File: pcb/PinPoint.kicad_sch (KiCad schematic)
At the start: 2 parts, among them U1 E73-2G4M08S-52833

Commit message: Create board outline, change battery holder
Signed-off-by: Devnol <pgkoutsoumanis@gmail.com>
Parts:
- BT1: footprint Battery:BatteryHolder_Multicomp_BC-2001_1x2032 -> Battery:BatteryHolder_Keystone_3034_1x20mm
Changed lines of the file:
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@@
 			)
 		)
-		(property "Footprint" "Battery:BatteryHolder_Multicomp_BC-2001_1x2032"
+		(property "Footprint" "Battery:BatteryHolder_Keystone_3034_1x20mm"
 			(at 59.69 84.836 90)
 			(effects

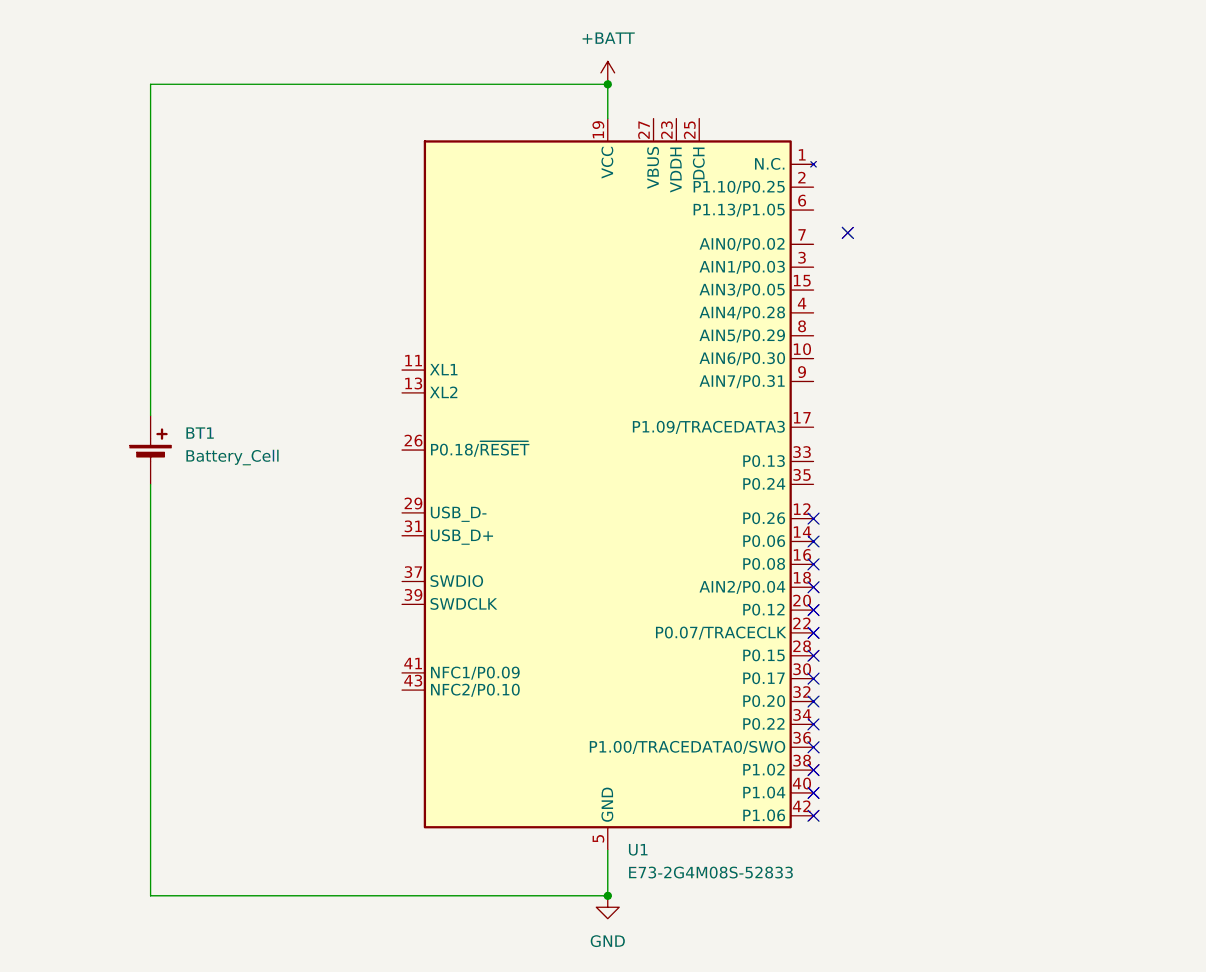
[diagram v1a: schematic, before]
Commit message: Add screw holes, debug port
Signed-off-by: Devnol <pgkoutsoumanis@gmail.com>
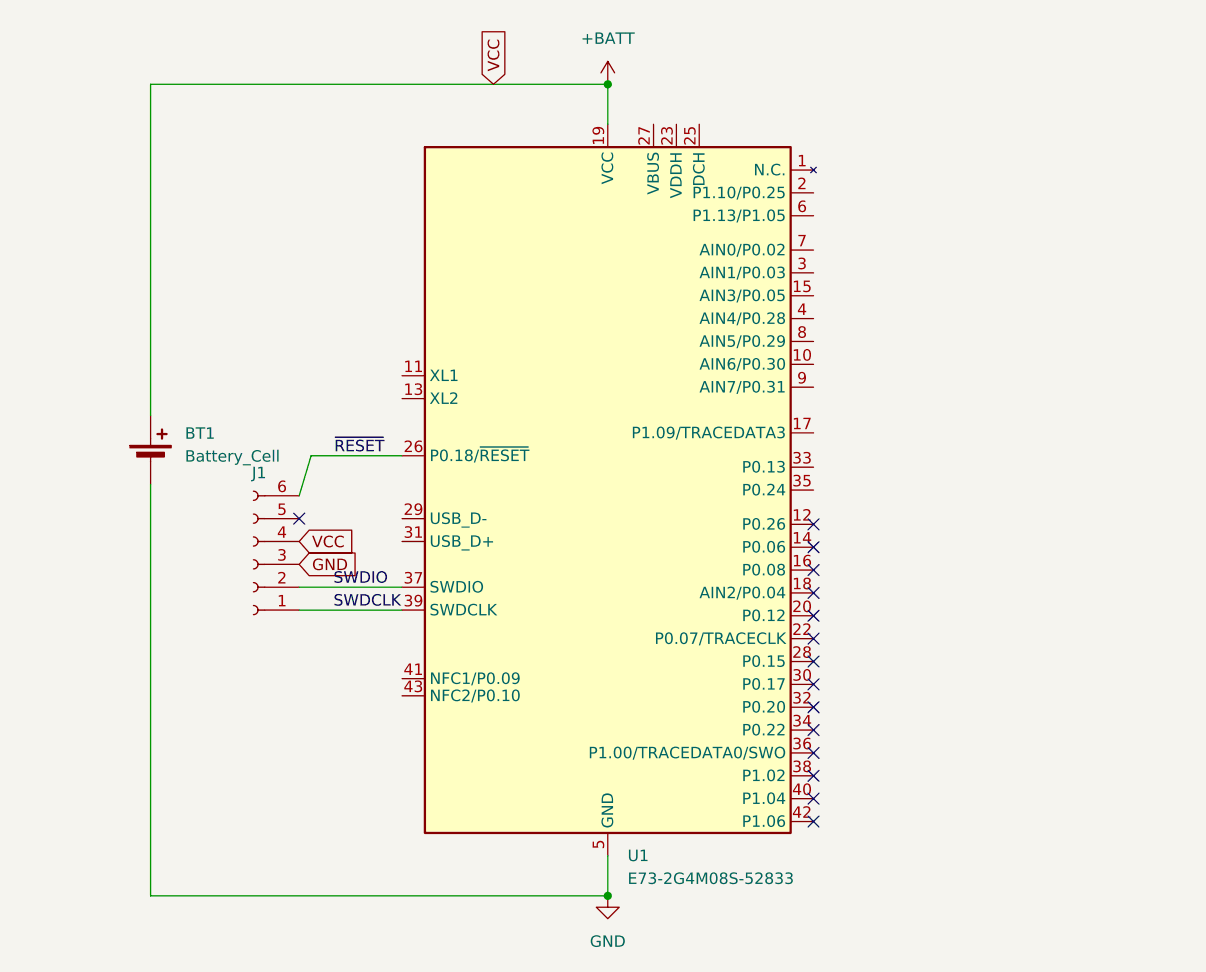
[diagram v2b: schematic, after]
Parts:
- added J1: ~, Connector_PinHeader_2.54mm:PinHeader_2x03_P2.54mm_Horizontal, symbol Connector:Conn_01x06_Socket
- U1: IC Datasheet (none) -> ${KIPRJMOD}/../docs/nRF52833_PS_v1.7.pdf
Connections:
- net +BATT: now also J1.4 (Pin_4)
- net GND: now also J1.3 (Pin_3)
- net ~{RESET}: now reaches U1.26 (P0.18/~{RESET})
- net ~{RESET}: now also J1.6 (Pin_6)
- net SWDIO: now reaches U1.37 (SWDIO)
- net SWDIO: now also J1.2 (Pin_2)
- net SWDCLK: now reaches U1.39 (SWDCLK)
- net SWDCLK: now also J1.1 (Pin_1)
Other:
- moved on the sheet: U1

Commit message: Add buzzer, include todo list for board features
Signed-off-by: Devnol <pgkoutsoumanis@gmail.com>
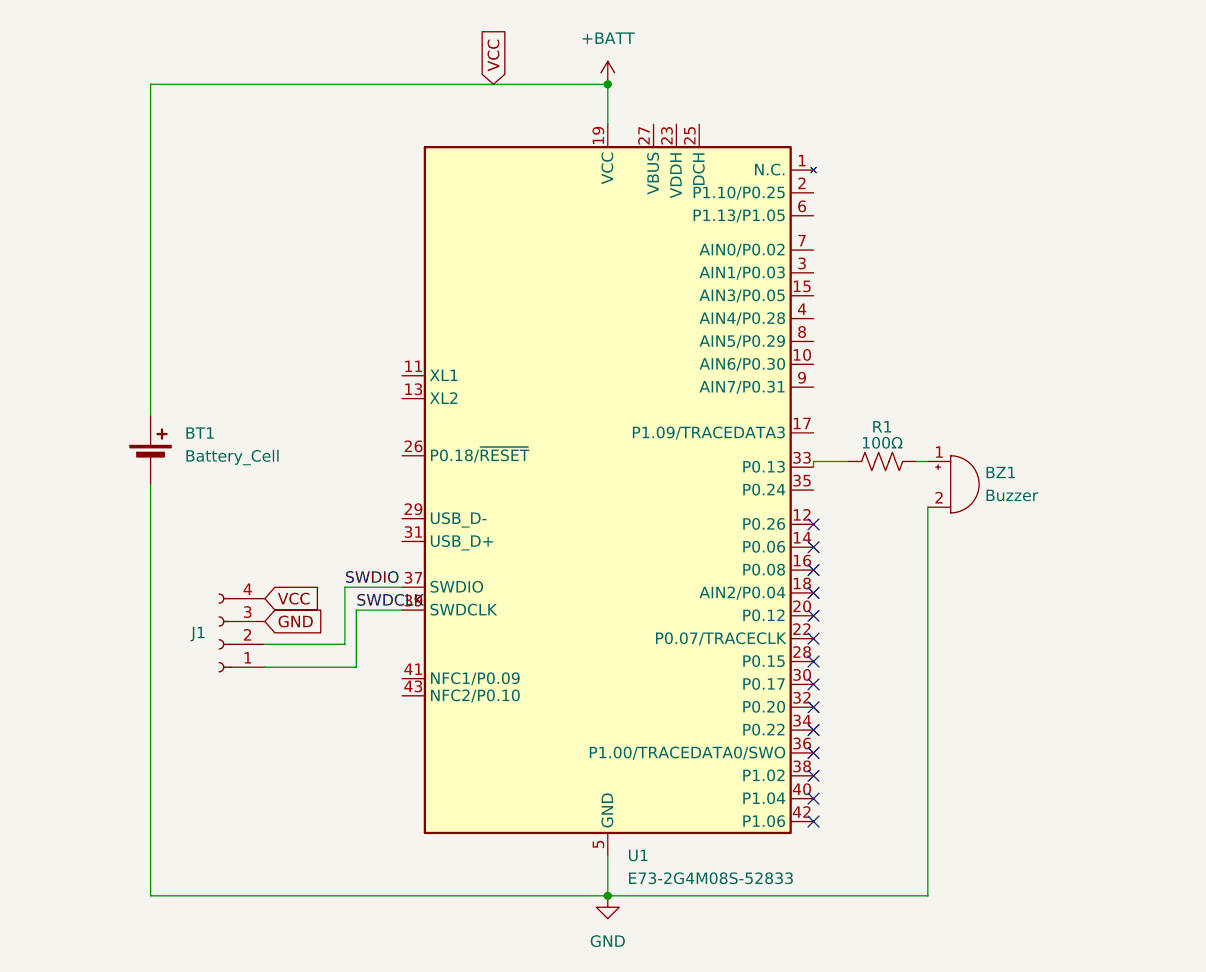
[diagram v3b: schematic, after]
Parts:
- added BZ1: Buzzer, Buzzer_Beeper:Buzzer_Murata_PKMCS0909E, symbol Device:Buzzer
- added R1: 100Ω, Resistor_SMD:R_0603_1608Metric, symbol Device:R_US
- J1: footprint Connector_PinHeader_2.54mm:PinHeader_2x03_P2.54mm_Horizontal -> Connector_PinHeader_2.54mm:PinHeader_1x04_P2.54mm_Vertical; symbol Connector:Conn_01x06_Socket -> Connector:Conn_01x04_Socket
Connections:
- net GND: now also BZ1.2 (-)
- net at U1.33 (P0.13): now also R1.1
- net ~{RESET}: no longer names the net of U1.26 (P0.18/~{RESET})
- net ~{RESET}: no longer J1.6 (Pin_6)
- new net: BZ1.1 (+), R1.2
- no-connect marks 15 -> 14
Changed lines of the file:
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@@
-	)
-	(no_connect
-		(at 76.2 92.71)
 	)
 	(no_connect
@@
 	(wire
 		(pts
-			(xy 77.5257 85.725) (xy 87.63 85.725)
+			(xy 82.55 109.22) (xy 82.55 102.87)
+		)
+		(stroke
+			(width 0)
+			(type default)
+		)
+	)
+	(wire
+		(pts
+			(xy 82.55 102.87) (xy 87.63 102.87)
 		)
 		(stroke
@@
 	(wire
 		(pts
-			(xy 77.5257 85.725) (xy 76.2 90.17)
-		)
-		(stroke
-			(width 0)
-			(type default)
-		)
-	)
-	(wire
-		(pts
 			(xy 59.69 81.28) (xy 59.69 44.45)
 		)
@@
 	(wire
 		(pts
+			(xy 81.28 106.68) (xy 81.28 100.33)
+		)
+		(stroke
+			(width 0)
+			(type default)
+		)
+	)
+	(wire
+		(pts
+			(xy 133.35 86.36) (xy 133.35 86.995)
+		)
+		(stroke
+			(width 0)
+			(type default)
+		)
+	)
+	(wire
+		(pts
+			(xy 144.78 86.36) (xy 146.05 86.36)
+		)
+		(stroke
+			(width 0)
+			(type default)
+		)
+	)
+	(wire
+		(pts
 			(xy 59.69 134.62) (xy 110.49 134.62)
 		)
@@
 	(wire
 		(pts
+			(xy 146.05 134.62) (xy 110.49 134.62)
+		)
+		(stroke
+			(width 0)
+			(type default)
+		)
+	)
+	(wire
+		(pts
 			(xy 110.49 134.62) (xy 110.49 130.175)
 		)
@@
 	(wire
 		(pts
-			(xy 76.2 102.87) (xy 87.63 102.87)
+			(xy 72.39 109.22) (xy 82.55 109.22)
 		)
 		(stroke
@@
 	(wire
 		(pts
-			(xy 76.2 100.33) (xy 87.63 100.33)
+			(xy 81.28 100.33) (xy 87.63 100.33)
+		)
+		(stroke
+			(width 0)
+			(type default)
+		)
+	)
+	(wire
+		(pts
+			(xy 72.39 106.68) (xy 81.28 106.68)
+		)
+		(stroke
+			(width 0)
+			(type default)
+		)
+	)
+	(wire
+		(pts
+			(xy 146.05 91.44) (xy 146.05 134.62)
+		)
+		(stroke
+			(width 0)
+			(type default)
+		)
+	)
+	(wire
+		(pts
+			(xy 133.35 86.36) (xy 137.16 86.36)
 		)
 		(stroke
@@
 	)
 	(label "SWDCLK"
-		(at 80.01 102.87 0)
+		(at 82.55 102.87 0)
 		(fields_autoplaced yes)
 		(effects
@@
 	)
 	(label "SWDIO"
-		(at 80.01 100.33 0)
+		(at 81.28 100.33 0)
 		(fields_autoplaced yes)
 		(effects
@@
 		)
 	)
-	(label "~{RESET}"
-		(at 80.0916 85.725 0)
+	(global_label "GND"
+		(shape input)
+		(at 72.39 104.14 0)
 		(fields_autoplaced yes)
 		(effects
@@
 				(size 1.27 1.27)
 			)
-			(justify left bottom)
-		)
-	)
-	(global_label "GND"
+			(justify left)
+		)
+		(property "Intersheetrefs" "${INTERSHEET_REFS}"
+			(at 79.2457 104.14 0)
+			(effects
+				(font
+					(size 1.27 1.27)
+				)
+				(justify left)
+				(hide yes)
+			)
+		)
+	)
+	(global_label "VCC"
 		(shape input)
-		(at 76.2 97.79 0)
+		(at 97.79 44.45 90)
 		(fields_autoplaced yes)
 		(effects
@@
 		)
 		(property "Intersheetrefs" "${INTERSHEET_REFS}"
-			(at 83.0557 97.79 0)
+			(at 97.79 37.8362 90)
 			(effects
 				(font
@@
 	(global_label "VCC"
 		(shape input)
-		(at 97.79 44.45 90)
+		(at 72.39 101.6 0)
 		(fields_autoplaced yes)
 		(effects
@@
 		)
 		(property "Intersheetrefs" "${INTERSHEET_REFS}"
-			(at 97.79 37.8362 90)
+			(at 79.0038 101.6 0)
 			(effects
 				(font
@@
 		)
 	)
-	(global_label "VCC"
-		(shape input)
-		(at 76.2 95.25 0)
-		(fields_autoplaced yes)
-		(effects
-			(font
-				(size 1.27 1.27)
-			)
-			(justify left)
-		)
-		(property "Intersheetrefs" "${INTERSHEET_REFS}"
-			(at 82.8138 95.25 0)
+	(symbol
+		(lib_id "Device:R_US")
+		(at 140.97 86.36 90)
+		(unit 1)
+		(exclude_from_sim no)
+		(in_bom yes)
+		(on_board yes)
+		(dnp no)
+		(property "Reference" "R1"
+			(at 140.97 82.55 90)
+			(effects
+				(font
+					(size 1.27 1.27)
+				)
+			)
+		)
+		(property "Value" "100Ω"
+			(at 140.97 84.328 90)
+			(effects
+				(font
+					(size 1.27 1.27)
+				)
+			)
+		)
+		(property "Footprint" "Resistor_SMD:R_0603_1608Metric"
+			(at 141.224 85.344 90)
+			(effects
+				(font
+					(size 1.27 1.27)
+				)
+				(hide yes)
+			)
+		)
+		(property "Datasheet" "~"
+			(at 140.97 86.36 0)
+			(effects
+				(font
+					(size 1.27 1.27)
+				)
+				(hide yes)
+			)
+		)
+		(property "Description" "Resistor, US symbol"
+			(at 140.97 86.36 0)
+			(effects
+				(font
+					(size 1.27 1.27)
+				)
+				(hide yes)
+			)
+		)
+		(pin "2"
+		)
+		(pin "1"
+		)
+		(instances
+			(project ""
+				(path "/cd1943be-3de8-48d0-ac34-bcd8bf7ade3c"
+					(reference "R1")
+					(unit 1)
+				)
+			)
+		)
+	)
+	(symbol
+		(lib_id "Device:Buzzer")
+		(at 148.59 88.9 0)
+		(unit 1)
+		(exclude_from_sim no)
+		(in_bom yes)
+		(on_board yes)
+		(dnp no)
+		(fields_autoplaced yes)
+		(property "Reference" "BZ1"
+			(at 152.4 87.6299 0)
 			(effects
 				(font
@@
 				)
 				(justify left)
-				(hide yes)
+			)
+		)
+		(property "Value" "Buzzer"
+			(at 152.4 90.1699 0)
+			(effects
+				(font
+					(size 1.27 1.27)
+				)
+				(justify left)
+			)
+		)
+		(property "Footprint" "Buzzer_Beeper:Buzzer_Murata_PKMCS0909E"
+			(at 147.955 86.36 90)
+			(effects
+				(font
+					(size 1.27 1.27)
+				)
+				(hide yes)
+			)
+		)
+		(property "Datasheet" "~"
+			(at 147.955 86.36 90)
+			(effects
+				(font
+					(size 1.27 1.27)
+				)
+				(hide yes)
+			)
+		)
+		(property "Description" "Buzzer, polarized"
+			(at 148.59 88.9 0)
+			(effects
+				(font
+					(size 1.27 1.27)
+				)
+				(hide yes)
+			)
+		)
+		(pin "2"
+		)
+		(pin "1"
+		)
+		(instances
+			(project ""
+				(path "/cd1943be-3de8-48d0-ac34-bcd8bf7ade3c"
+					(reference "BZ1")
+					(unit 1)
+				)
 			)
 		)
@@
 	)
 	(symbol
-		(lib_id "Connector:Conn_01x06_Socket")
-		(at 71.12 97.79 180)
+		(lib_id "Connector:Conn_01x04_Socket")
+		(at 67.31 106.68 180)
 		(unit 1)
 		(exclude_from_sim no)
@@
 		(on_board yes)
 		(dnp no)
-		(fields_autoplaced yes)
 		(property "Reference" "J1"
-			(at 71.755 87.63 0)
+			(at 65.024 105.41 0)
 			(effects
 				(font
@@
 		)
 		(property "Value" "~"
-			(at 77.47 96.5201 0)
-			(effects
-				(font
-					(size 1.27 1.27)
-				)
-				(justify right)
-			)
-		)
-		(property "Footprint" "Connector_PinHeader_2.54mm:PinHeader_2x03_P2.54mm_Horizontal"
-			(at 71.12 97.79 0)
+			(at 67.945 99.06 0)
+			(effects
+				(font
+					(size 1.27 1.27)
+				)
+			)
+		)
+		(property "Footprint" "Connector_PinHeader_2.54mm:PinHeader_1x04_P2.54mm_Vertical"
+			(at 67.31 106.68 0)
 			(effects
 				(font
@@
 		)
 		(property "Datasheet" "~"
-			(at 71.12 97.79 0)
-			(effects
-				(font
-					(size 1.27 1.27)
-				)
-				(hide yes)
-			)
-		)
-		(property "Description" "Generic connector, single row, 01x06, script generated"
-			(at 71.12 97.79 0)
+			(at 67.31 106.68 0)
+			(effects
+				(font
+					(size 1.27 1.27)
+				)
+				(hide yes)
+			)
+		)
+		(property "Description" "Generic connector, single row, 01x04, script generated"
+			(at 67.31 106.68 0)
 			(effects
 				(font
@@
 		(pin "1"
 		)
-		(pin "5"
-		)
-		(pin "6"
-		)
 		(instances

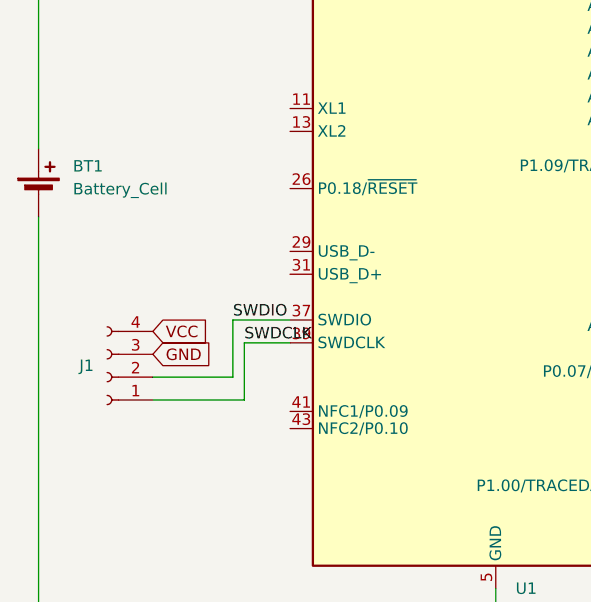
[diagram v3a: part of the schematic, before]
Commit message: Jankily add microUSB port
Signed-off-by: Devnol <pgkoutsoumanis@gmail.com>
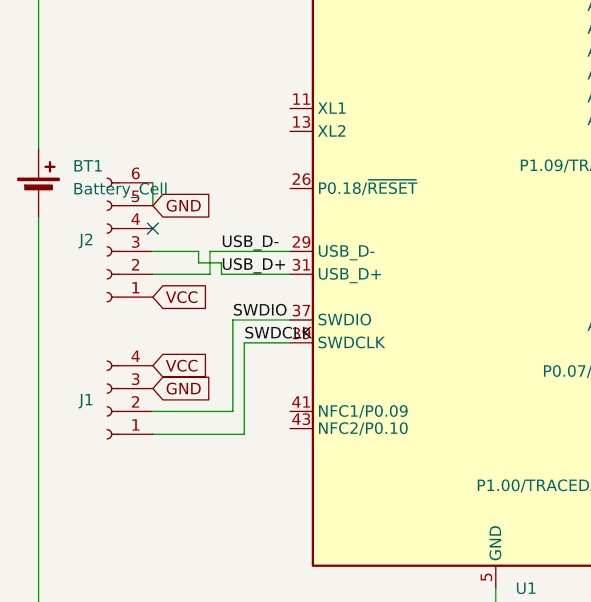
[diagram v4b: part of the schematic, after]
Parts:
- added J2: ~, Connector_USB:USB_Micro-B_Molex_47346-0001, symbol Connector:Conn_01x06_Socket
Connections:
- net +BATT: now also J2.1 (Pin_1)
- net GND: now also J2.5 (Pin_5), J2.6 (Pin_6)
- net USB_D-: now reaches U1.29 (USB_D-)
- net USB_D-: now also J2.2 (Pin_2)
- net USB_D+: now reaches U1.31 (USB_D+)
- net USB_D+: now also J2.3 (Pin_3)
- no-connect marks 14 -> 15
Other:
- moved on the sheet: J1
